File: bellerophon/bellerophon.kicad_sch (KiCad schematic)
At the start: 34 parts, among them Q1 ST3413A, Q2 IRLL014NPBF, Q3 IRLL014NPBF, U1 HT7350-A, U2 Adafruit_ICM20948, U3 MPL3115A2, U4 Teensy4.0

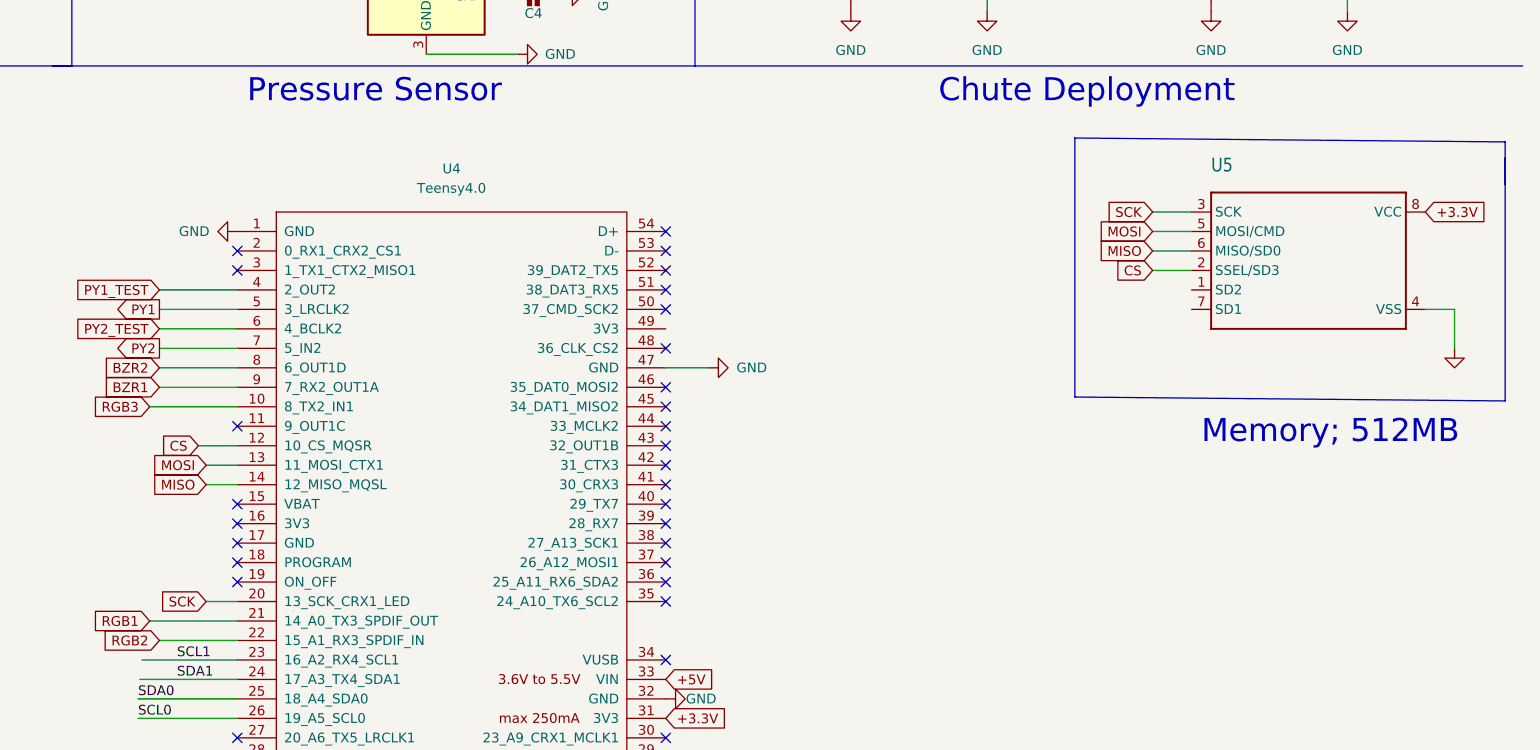
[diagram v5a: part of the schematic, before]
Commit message: Modify schematic for SMT Flash chip
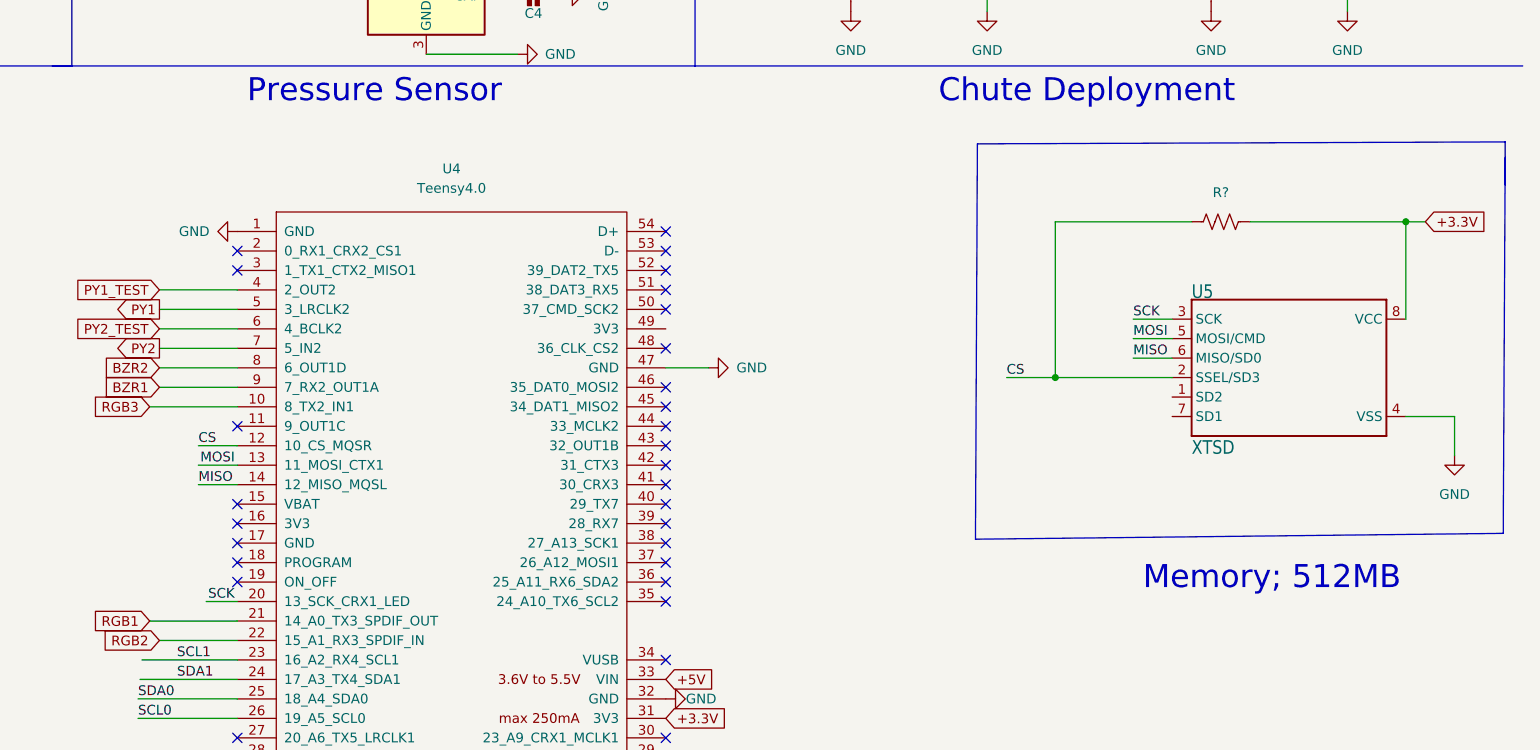
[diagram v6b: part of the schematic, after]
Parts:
- added R?: (no value), Resistor_SMD:R_1206_3216Metric_Pad1.30x1.75mm_HandSolder, symbol Device:R_US
- U5: value (none) -> XTSD; footprint (none) -> Adafruit SPI Flash SD Card:LGA8_8X6
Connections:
- net +3.3V: now also R?.1
- net CS: now also R?.2
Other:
- moved on the sheet: U5

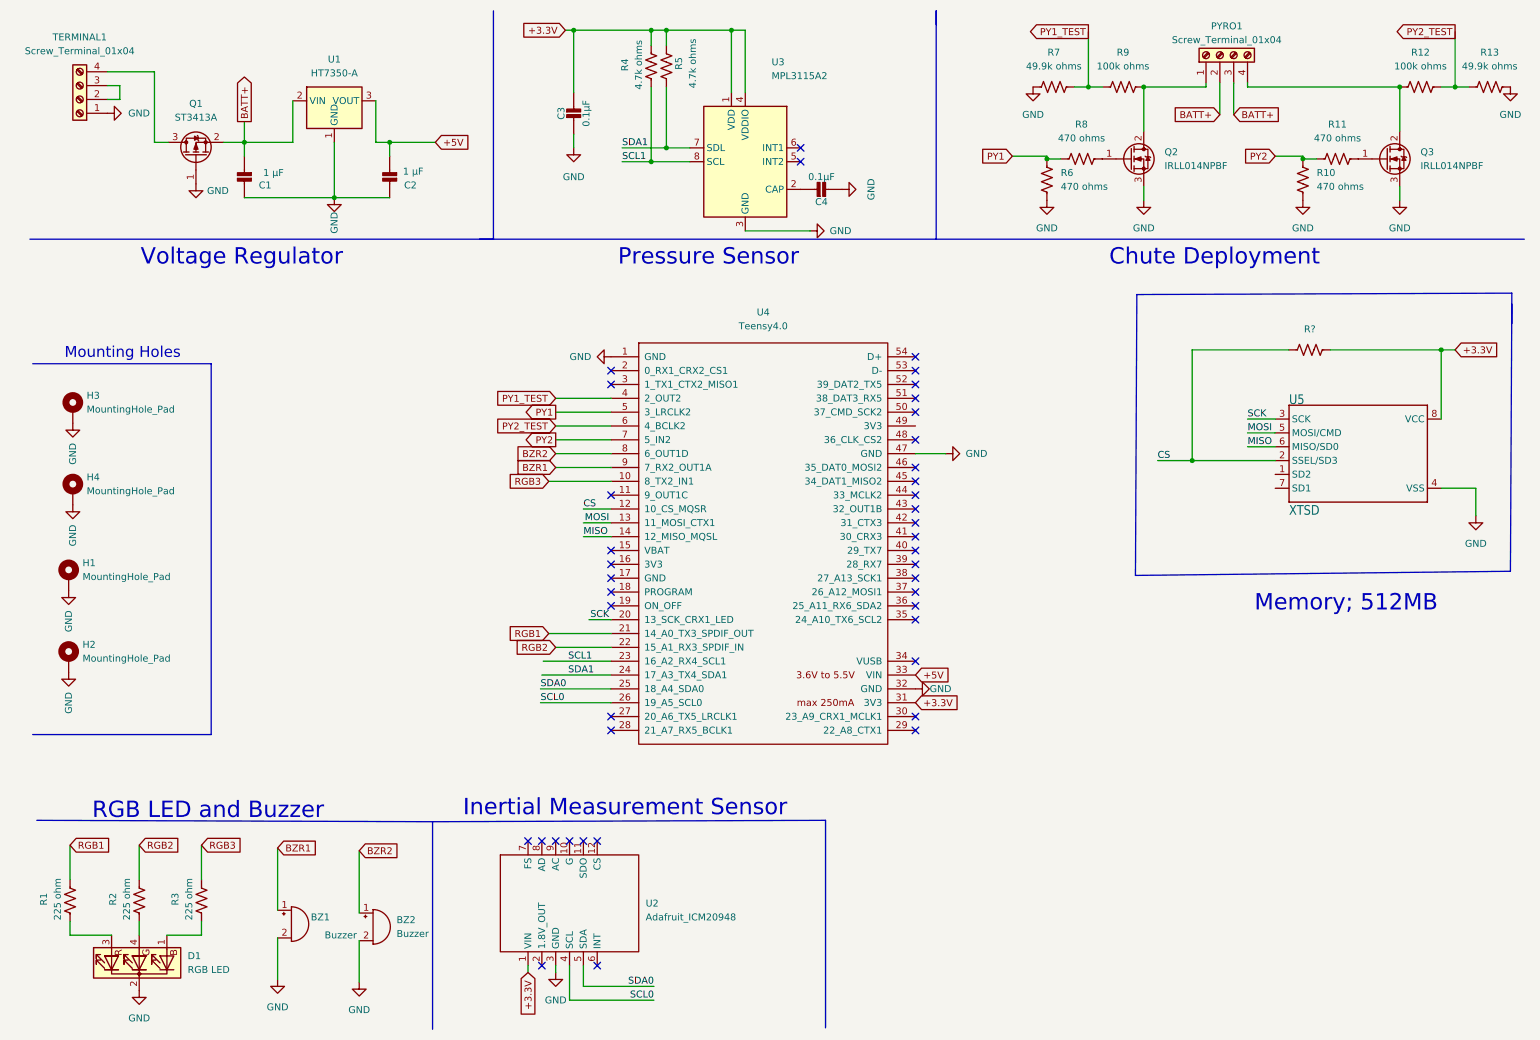
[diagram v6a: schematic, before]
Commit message: remove second buzzer
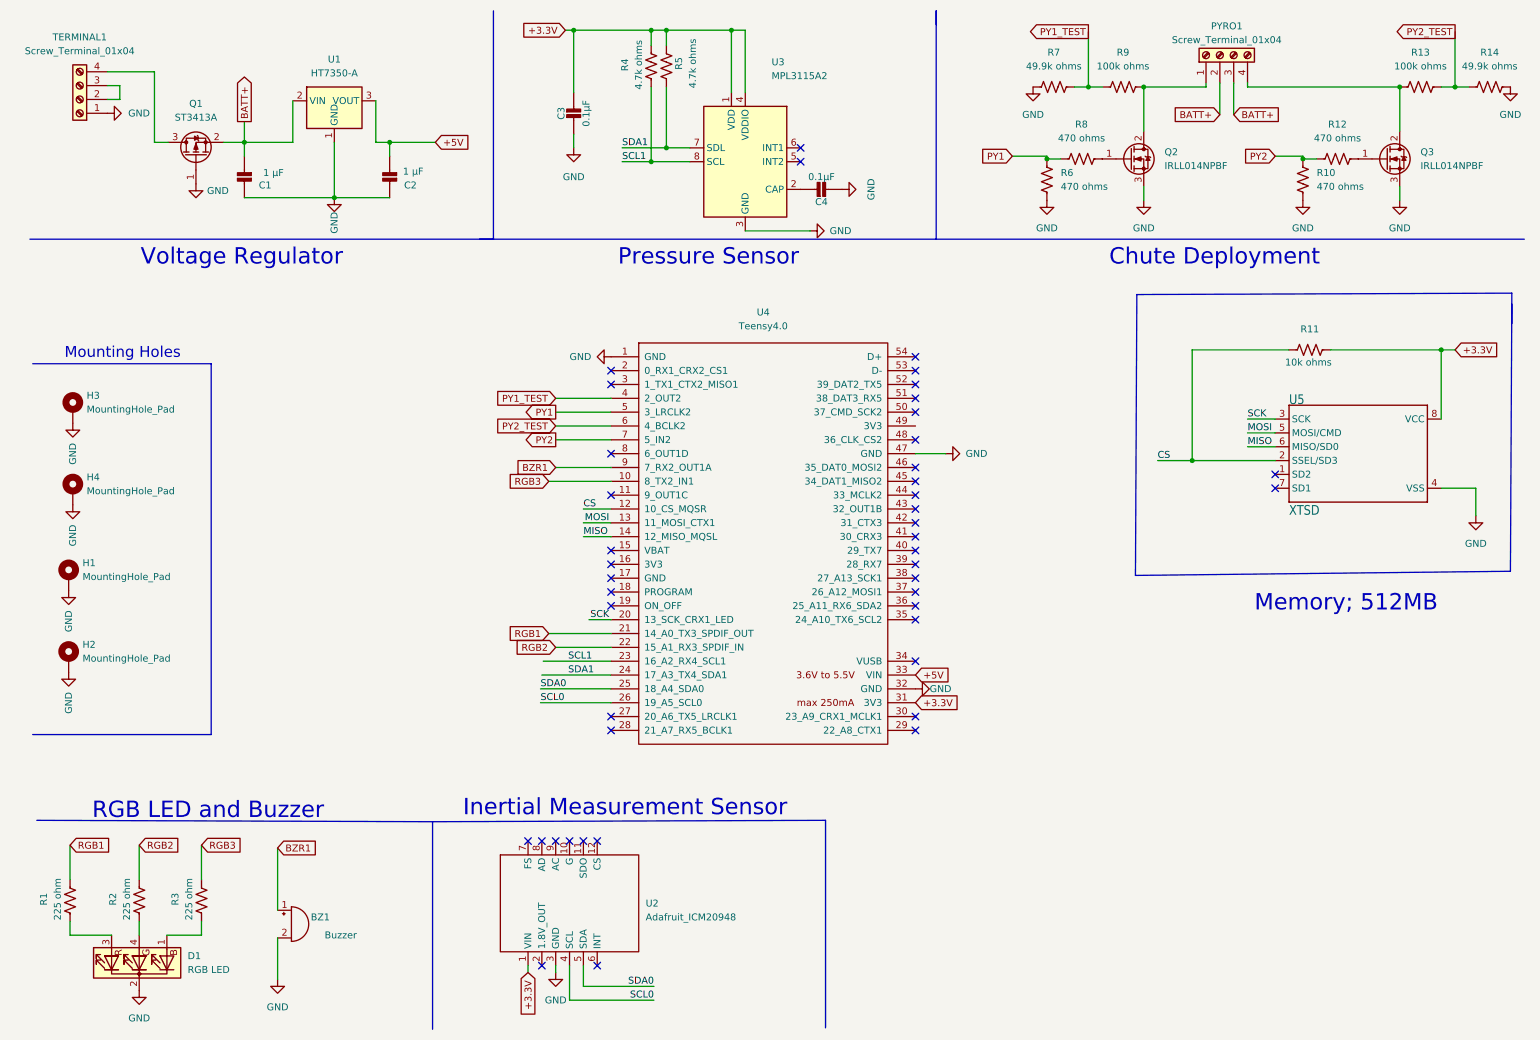
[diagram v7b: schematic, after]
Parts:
- removed BZ2: Buzzer, Buzzer:PiezoBuzzer-PS1240, symbol Device:Buzzer
- R11: renamed from R?; value (none) -> 10k ohms
- U5: footprint Adafruit SPI Flash SD Card:LGA8_8X6 -> XTSD:LGA8_8X6
- renumbered R11 to R12, R12 to R13, R13 to R14
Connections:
- net BZR2: no longer names the net of U4.8 (6_OUT1D)
- no-connect marks 41 -> 44
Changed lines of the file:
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@@
   (no_connect (at 118.11 120.65))
   (no_connect (at 152.908 39.116))
+  (no_connect (at 240.03 99.06))
   (no_connect (at 173.99 90.17))
   (no_connect (at 173.99 85.09))
@@
   (no_connect (at 118.11 77.47))
   (no_connect (at 118.11 80.01))
+  (no_connect (at 240.03 96.52))
   (no_connect (at 118.11 115.57))
   (no_connect (at 113.03 163.83))
@@
   (no_connect (at 102.87 163.83))
   (no_connect (at 115.57 186.69))
+  (no_connect (at 118.11 92.71))
   (no_connect (at 115.57 163.83))
   (no_connect (at 152.908 36.576))
@@
     (stroke (width 0) (type default) (color 0 0 0 0))
   )
-  (wire (pts (xy 71.882 165.608) (xy 71.882 177.038))
-    (stroke (width 0) (type default) (color 0 0 0 0))
-  )
   (wire (pts (xy 105.41 133.35) (xy 118.11 133.35))
     (stroke (width 0) (type default) (color 0 0 0 0))
@@
     (stroke (width 0) (type default) (color 0 0 0 0))
   )
-  (wire (pts (xy 107.95 92.71) (xy 118.11 92.71))
-    (stroke (width 0) (type default) (color 0 0 0 0))
-  )
   (wire (pts (xy 59.69 35.56) (xy 50.8 35.56))
     (stroke (width 0) (type default) (color 0 0 0 0))
@@
   )
   (wire (pts (xy 74.93 27.94) (xy 74.93 35.56))
-    (stroke (width 0) (type default) (color 0 0 0 0))
-  )
-  (wire (pts (xy 71.882 182.118) (xy 71.882 189.738))
     (stroke (width 0) (type default) (color 0 0 0 0))
   )
@@
     (effects (font (size 1.27 1.27)) (justify left))
     (property "Intersheet References" "${INTERSHEET_REFS}" (id 0) (at 92.1356 35.6394 0)
-      (effects (font (size 1.27 1.27)) (justify left) hide)
-    )
-  )
-  (global_label "BZR2" (shape input) (at 107.95 92.71 180) (fields_autoplaced)
-    (effects (font (size 1.27 1.27)) (justify right))
-    (property "Intersheet References" "${INTERSHEET_REFS}" (id 0) (at 100.5779 92.6306 0)
-      (effects (font (size 1.27 1.27)) (justify right) hide)
-    )
-  )
-  (global_label "BZR2" (shape input) (at 71.882 165.608 0) (fields_autoplaced)
-    (effects (font (size 1.27 1.27)) (justify left))
-    (property "Intersheet References" "${INTERSHEET_REFS}" (id 0) (at 79.2541 165.5286 0)
       (effects (font (size 1.27 1.27)) (justify left) hide)
     )
@@
       (effects (font (size 1.778 1.5113)) (justify left bottom))
     )
-    (property "Footprint" "Adafruit SPI Flash SD Card:LGA8_8X6" (id 2) (at 255.27 93.98 0)
+    (property "Footprint" "XTSD:LGA8_8X6" (id 2) (at 255.27 93.98 0)
       (effects (font (size 1.27 1.27)) hide)
     )
@@
   (symbol (lib_id "power:GND") (at 276.86 104.14 0) (unit 1)
     (in_bom yes) (on_board yes) (fields_autoplaced)
-    (property "Reference" "#PWR?" (id 0) (at 276.86 110.49 0)
+    (property "Reference" "#PWR023" (id 0) (at 276.86 110.49 0)
       (effects (font (size 1.27 1.27)) hide)
     )
@@
   (symbol (lib_id "Device:R_US") (at 251.46 38.608 90) (unit 1)
     (in_bom yes) (on_board yes) (fields_autoplaced)
-    (property "Reference" "R11" (id 0) (at 251.46 32.258 90))
+    (property "Reference" "R12" (id 0) (at 251.46 32.258 90))
     (property "Value" "470 ohms" (id 1) (at 251.46 34.798 90))
     (property "Footprint" "Resistor_SMD:R_1206_3216Metric_Pad1.30x1.75mm_HandSolder" (id 2) (at 251.714 37.592 90)
@@
     (pin "2")
   )
-  (symbol (lib_id "power:GND") (at 71.882 189.738 0) (unit 1)
-    (in_bom yes) (on_board yes) (fields_autoplaced)
-    (property "Reference" "#PWR010" (id 0) (at 71.882 196.088 0)
-      (effects (font (size 1.27 1.27)) hide)
-    )
-    (property "Value" "GND" (id 1) (at 71.882 194.818 0))
-    (property "Footprint" "" (id 2) (at 71.882 189.738 0)
-      (effects (font (size 1.27 1.27)) hide)
-    )
-    (property "Datasheet" "" (id 3) (at 71.882 189.738 0)
-      (effects (font (size 1.27 1.27)) hide)
-    )
-    (pin "1")
-  )
   (symbol (lib_id "power:GND") (at 31.496 191.262 0) (unit 1)
     (in_bom yes) (on_board yes) (fields_autoplaced)
@@
   (symbol (lib_id "Device:R_US") (at 266.7 25.4 90) (unit 1)
     (in_bom yes) (on_board yes) (fields_autoplaced)
-    (property "Reference" "R12" (id 0) (at 266.7 19.05 90))
+    (property "Reference" "R13" (id 0) (at 266.7 19.05 90))
     (property "Value" "100k ohms" (id 1) (at 266.7 21.59 90))
     (property "Footprint" "Resistor_SMD:R_1206_3216Metric_Pad1.30x1.75mm_HandSolder" (id 2) (at 266.954 24.384 90)
@@
   (symbol (lib_id "Device:R_US") (at 279.4 25.4 90) (unit 1)
     (in_bom yes) (on_board yes) (fields_autoplaced)
-    (property "Reference" "R13" (id 0) (at 279.4 19.05 90))
+    (property "Reference" "R14" (id 0) (at 279.4 19.05 90))
     (property "Value" "49.9k ohms" (id 1) (at 279.4 21.59 90))
     (property "Footprint" "Resistor_SMD:R_1206_3216Metric_Pad1.30x1.75mm_HandSolder" (id 2) (at 279.654 24.384 90)
@@
     )
     (property "Datasheet" "" (id 3) (at 50.8 40.64 0)
-      (effects (font (size 1.27 1.27)) hide)
-    )
-    (pin "1")
-    (pin "2")
-  )
-  (symbol (lib_id "Device:Buzzer") (at 74.422 179.578 0) (unit 1)
-    (in_bom yes) (on_board yes) (fields_autoplaced)
-    (property "Reference" "BZ2" (id 0) (at 78.74 178.3079 0)
-      (effects (font (size 1.27 1.27)) (justify left))
-    )
-    (property "Value" "Buzzer" (id 1) (at 78.74 180.8479 0)
-      (effects (font (size 1.27 1.27)) (justify left))
-    )
-    (property "Footprint" "Buzzer:PiezoBuzzer-PS1240" (id 2) (at 73.787 177.038 90)
-      (effects (font (size 1.27 1.27)) hide)
-    )
-    (property "Datasheet" "~" (id 3) (at 73.787 177.038 90)
       (effects (font (size 1.27 1.27)) hide)
     )
@@
   (symbol (lib_id "Device:R_US") (at 246.38 73.66 270) (unit 1)
     (in_bom yes) (on_board yes)
-    (property "Reference" "R?" (id 0) (at 246.38 69.85 90))
-    (property "Value" "" (id 1) (at 246.126 75.946 90))
+    (property "Reference" "R11" (id 0) (at 246.38 69.85 90))
+    (property "Value" "10k ohms" (id 1) (at 246.126 75.946 90))
     (property "Footprint" "Resistor_SMD:R_1206_3216Metric_Pad1.30x1.75mm_HandSolder" (id 2) (at 246.126 74.676 90)
       (effects (font (size 1.27 1.27)) hide)
@@
   (symbol (lib_id "power:GND") (at 262.89 46.228 0) (unit 1)
     (in_bom yes) (on_board yes) (fields_autoplaced)
-    (property "Reference" "#PWR023" (id 0) (at 262.89 52.578 0)
+    (property "Reference" "#PWR022" (id 0) (at 262.89 52.578 0)
       (effects (font (size 1.27 1.27)) hide)
     )
@@
       (reference "#PWR09") (unit 1) (value "GND") (footprint "")
     )
-    (path "/80881318-82e5-40d7-b92d-c41a41b7e7f9"
-      (reference "#PWR010") (unit 1) (value "GND") (footprint "")
-    )
     (path "/0fd9c5ac-c3f0-4510-81b6-a53abab940bf"
       (reference "#PWR011") (unit 1) (value "GND") (footprint "")
@@
     )
     (path "/f6a96f3c-ab94-4454-9c87-735341c02940"
+      (reference "#PWR022") (unit 1) (value "GND") (footprint "")
+    )
+    (path "/4bcda94a-db47-433f-a0ca-0aa4d3357647"
       (reference "#PWR023") (unit 1) (value "GND") (footprint "")
     )
@@
       (reference "#PWR024") (unit 1) (value "GND") (footprint "")
     )
-    (path "/4bcda94a-db47-433f-a0ca-0aa4d3357647"
-      (reference "#PWR?") (unit 1) (value "GND") (footprint "")
-    )
     (path "/8a393ed2-cfe0-4f0f-9490-ab6f8e39e2cc"
       (reference "BZ1") (unit 1) (value "Buzzer") (footprint "Buzzer:PiezoBuzzer-PS1240")
     )
-    (path "/b963fd24-0780-4680-8614-fe86ef253063"
-      (reference "BZ2") (unit 1) (value "Buzzer") (footprint "Buzzer:PiezoBuzzer-PS1240")
-    )
     (path "/b8650d51-eff7-4c07-9f39-e52b608b61ce"
       (reference "C1") (unit 1) (value "1 µF") (footprint "Capacitor_SMD:C_0805_2012Metric_Pad1.18x1.45mm_HandSolder")
@@
       (reference "R10") (unit 1) (value "470 ohms") (footprint "Resistor_SMD:R_1206_3216Metric_Pad1.30x1.75mm_HandSolder")
     )
+    (path "/cdd8ac69-37b5-44ae-89e8-7a1b9fce26ca"
+      (reference "R11") (unit 1) (value "10k ohms") (footprint "Resistor_SMD:R_1206_3216Metric_Pad1.30x1.75mm_HandSolder")
+    )
     (path "/6195d1a0-cede-4bde-9f18-71023388ad6d"
-      (reference "R11") (unit 1) (value "470 ohms") (footprint "Resistor_SMD:R_1206_3216Metric_Pad1.30x1.75mm_HandSolder")
+      (reference "R12") (unit 1) (value "470 ohms") (footprint "Resistor_SMD:R_1206_3216Metric_Pad1.30x1.75mm_HandSolder")
     )
     (path "/99fbcbc6-ea04-4e28-860d-35bb80025d15"
-      (reference "R12") (unit 1) (value "100k ohms") (footprint "Resistor_SMD:R_1206_3216Metric_Pad1.30x1.75mm_HandSolder")
+      (reference "R13") (unit 1) (value "100k ohms") (footprint "Resistor_SMD:R_1206_3216Metric_Pad1.30x1.75mm_HandSolder")
     )
     (path "/a91641b5-09f0-4dfe-afc4-08ca53819e29"
-      (reference "R13") (unit 1) (value "49.9k ohms") (footprint "Resistor_SMD:R_1206_3216Metric_Pad1.30x1.75mm_HandSolder")
-    )
-    (path "/cdd8ac69-37b5-44ae-89e8-7a1b9fce26ca"
-      (reference "R?") (unit 1) (value "10k ohms") (footprint "Resistor_SMD:R_1206_3216Metric_Pad1.30x1.75mm_HandSolder")
+      (reference "R14") (unit 1) (value "49.9k ohms") (footprint "Resistor_SMD:R_1206_3216Metric_Pad1.30x1.75mm_HandSolder")
     )
     (path "/a6785074-04ef-4659-a3ac-ebad7b1a7692"
@@
     )
     (path "/2f0f5f5b-f250-4fe1-9849-223336d00341"
-      (reference "U5") (unit 1) (value "XTSD") (footprint "Adafruit SPI Flash SD Card:LGA8_8X6")
-    )
-  )
+      (reference "U5") (unit 1) (value "XTSD") (footprint "XTSD:LGA8_8X6")
+    )
+  )
